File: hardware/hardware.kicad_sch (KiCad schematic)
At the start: 10 parts, among them U1 NE555P

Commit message: more research
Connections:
- net V_IN is gone; now on net KB_IN: C1.2, RV4.2, U1.5 (CV)
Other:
- note added: "555 VCO"
- note added: "Arduino Inputs"
- note added: "Keyboard simulator"
- moved on the sheet: RV4
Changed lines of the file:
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@@
     (stroke (width 0) (type default) (color 0 0 0 0))
   )
-  (wire (pts (xy 160.02 81.28) (xy 162.56 81.28))
+  (wire (pts (xy 168.275 67.945) (xy 170.815 67.945))
     (stroke (width 0) (type default) (color 0 0 0 0))
   )
@@
     (stroke (width 0) (type default) (color 0 0 0 0))
   )
+  (text "Keyboard simulator" (at 168.91 74.295 0)
+    (effects (font (size 1.27 1.27)) (justify left bottom))
+  )
+  (text "555 VCO\n" (at 74.93 86.995 0)
+    (effects (font (size 1.27 1.27)) (justify left bottom))
+  )
+  (text "Arduino Inputs" (at 85.09 26.035 0)
+    (effects (font (size 1.27 1.27)) (justify left bottom))
+  )
   (global_label "POT_REL" (shape input) (at 55.88 54.61 0) (fields_autoplaced)
     (effects (font (size 1.27 1.27)) (justify left))
@@
     )
   )
-  (global_label "V_IN" (shape input) (at 87.63 71.12 180) (fields_autoplaced)
+  (global_label "KB_IN" (shape input) (at 87.63 71.12 180) (fields_autoplaced)
     (effects (font (size 1.27 1.27)) (justify right))
-    (property "Intersheet References" "${INTERSHEET_REFS}" (id 0) (at 81.2255 71.0406 0)
+    (property "Intersheet References" "${INTERSHEET_REFS}" (id 0) (at 79.774 71.0406 0)
       (effects (font (size 1.27 1.27)) (justify right) hide)
     )
@@
     )
   )
-  (global_label "V_IN" (shape output) (at 162.56 81.28 0) (fields_autoplaced)
-    (effects (font (size 1.27 1.27)) (justify left))
-    (property "Intersheet References" "${INTERSHEET_REFS}" (id 0) (at 168.9645 81.2006 0)
+  (global_label "KB_IN" (shape output) (at 170.815 67.945 0) (fields_autoplaced)
+    (effects (font (size 1.27 1.27)) (justify left))
+    (property "Intersheet References" "${INTERSHEET_REFS}" (id 0) (at 178.671 67.8656 0)
       (effects (font (size 1.27 1.27)) (justify left) hide)
     )
@@
     )
   )
-  (symbol (lib_id "Device:R_Potentiometer") (at 156.21 81.28 0) (unit 1)
-    (in_bom yes) (on_board yes) (fields_autoplaced)
-    (property "Reference" "RV4" (id 0) (at 153.67 80.0099 0)
-      (effects (font (size 1.27 1.27)) (justify right))
-    )
-    (property "Value" ">10k" (id 1) (at 153.67 82.5499 0)
-      (effects (font (size 1.27 1.27)) (justify right))
-    )
-    (property "Footprint" "" (id 2) (at 156.21 81.28 0)
-      (effects (font (size 1.27 1.27)) hide)
-    )
-    (property "Datasheet" "~" (id 3) (at 156.21 81.28 0)
+  (symbol (lib_id "Device:R_Potentiometer") (at 164.465 67.945 0) (unit 1)
+    (in_bom yes) (on_board yes) (fields_autoplaced)
+    (property "Reference" "RV4" (id 0) (at 161.925 66.6749 0)
+      (effects (font (size 1.27 1.27)) (justify right))
+    )
+    (property "Value" ">10k" (id 1) (at 161.925 69.2149 0)
+      (effects (font (size 1.27 1.27)) (justify right))
+    )
+    (property "Footprint" "" (id 2) (at 164.465 67.945 0)
+      (effects (font (size 1.27 1.27)) hide)
+    )
+    (property "Datasheet" "~" (id 3) (at 164.465 67.945 0)
       (effects (font (size 1.27 1.27)) hide)
     )
@@
     (pin "1")
   )
-  (symbol (lib_id "power:VCC") (at 156.21 77.47 0) (unit 1)
-    (in_bom yes) (on_board yes) (fields_autoplaced)
-    (property "Reference" "#PWR?" (id 0) (at 156.21 81.28 0)
-      (effects (font (size 1.27 1.27)) hide)
-    )
-    (property "Value" "VCC" (id 1) (at 156.21 71.755 0))
-    (property "Footprint" "" (id 2) (at 156.21 77.47 0)
-      (effects (font (size 1.27 1.27)) hide)
-    )
-    (property "Datasheet" "" (id 3) (at 156.21 77.47 0)
+  (symbol (lib_id "power:VCC") (at 164.465 64.135 0) (unit 1)
+    (in_bom yes) (on_board yes) (fields_autoplaced)
+    (property "Reference" "#PWR?" (id 0) (at 164.465 67.945 0)
+      (effects (font (size 1.27 1.27)) hide)
+    )
+    (property "Value" "VCC" (id 1) (at 164.465 58.42 0))
+    (property "Footprint" "" (id 2) (at 164.465 64.135 0)
+      (effects (font (size 1.27 1.27)) hide)
+    )
+    (property "Datasheet" "" (id 3) (at 164.465 64.135 0)
       (effects (font (size 1.27 1.27)) hide)
     )
@@
     (pin "2")
   )
-  (symbol (lib_id "power:GND") (at 156.21 85.09 0) (unit 1)
-    (in_bom yes) (on_board yes) (fields_autoplaced)
-    (property "Reference" "#PWR?" (id 0) (at 156.21 91.44 0)
-      (effects (font (size 1.27 1.27)) hide)
-    )
-    (property "Value" "GND" (id 1) (at 156.21 90.17 0))
-    (property "Footprint" "" (id 2) (at 156.21 85.09 0)
-      (effects (font (size 1.27 1.27)) hide)
-    )
-    (property "Datasheet" "" (id 3) (at 156.21 85.09 0)
-      (effects (font (size 1.27 1.27)) hide)
-    )
+  (symbol (lib_id "power:GND") (at 164.465 71.755 0) (unit 1)
+    (in_bom yes) (on_board yes) (fields_autoplaced)
+    (property "Reference" "#PWR?" (id 0) (at 164.465 78.105 0)
+      (effects (font (size 1.27 1.27)) hide)
+    )
+    (property "Value" "GND" (id 1) (at 164.465 76.835 0))
+    (property "Footprint" "" (id 2) (at 164.465 71.755 0)
+      (effects (font (size 1.27 1.27)) hide)
+    )
+    (property "Datasheet" "" (id 3) (at 164.465 71.755 0)
+      (effects (font (size 1.27 1.27)) hide)
+    )

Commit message: more test schematics
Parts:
- added C4: 0.1u, symbol Device:C
- added C5: 10u, symbol Device:C
- added R9: KB_R, symbol Device:R_Variable
- added U2: NE555P, Package_DIP:DIP-8_W7.62mm, symbol Timer:NE555P
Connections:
- net GND: now also C4.1, C5.2, U2.1 (GND)
- net VCC: now also C4.2, U2.4 (R), U2.8 (VCC)
- new net: C5.1, R9.1, U2.2 (TR), U2.6 (THR)
- new net: R9.2, U2.3 (Q)
- no-connect marks 2 -> 4
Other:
- note added: "555 RCO"
- moved on the sheet: RV4

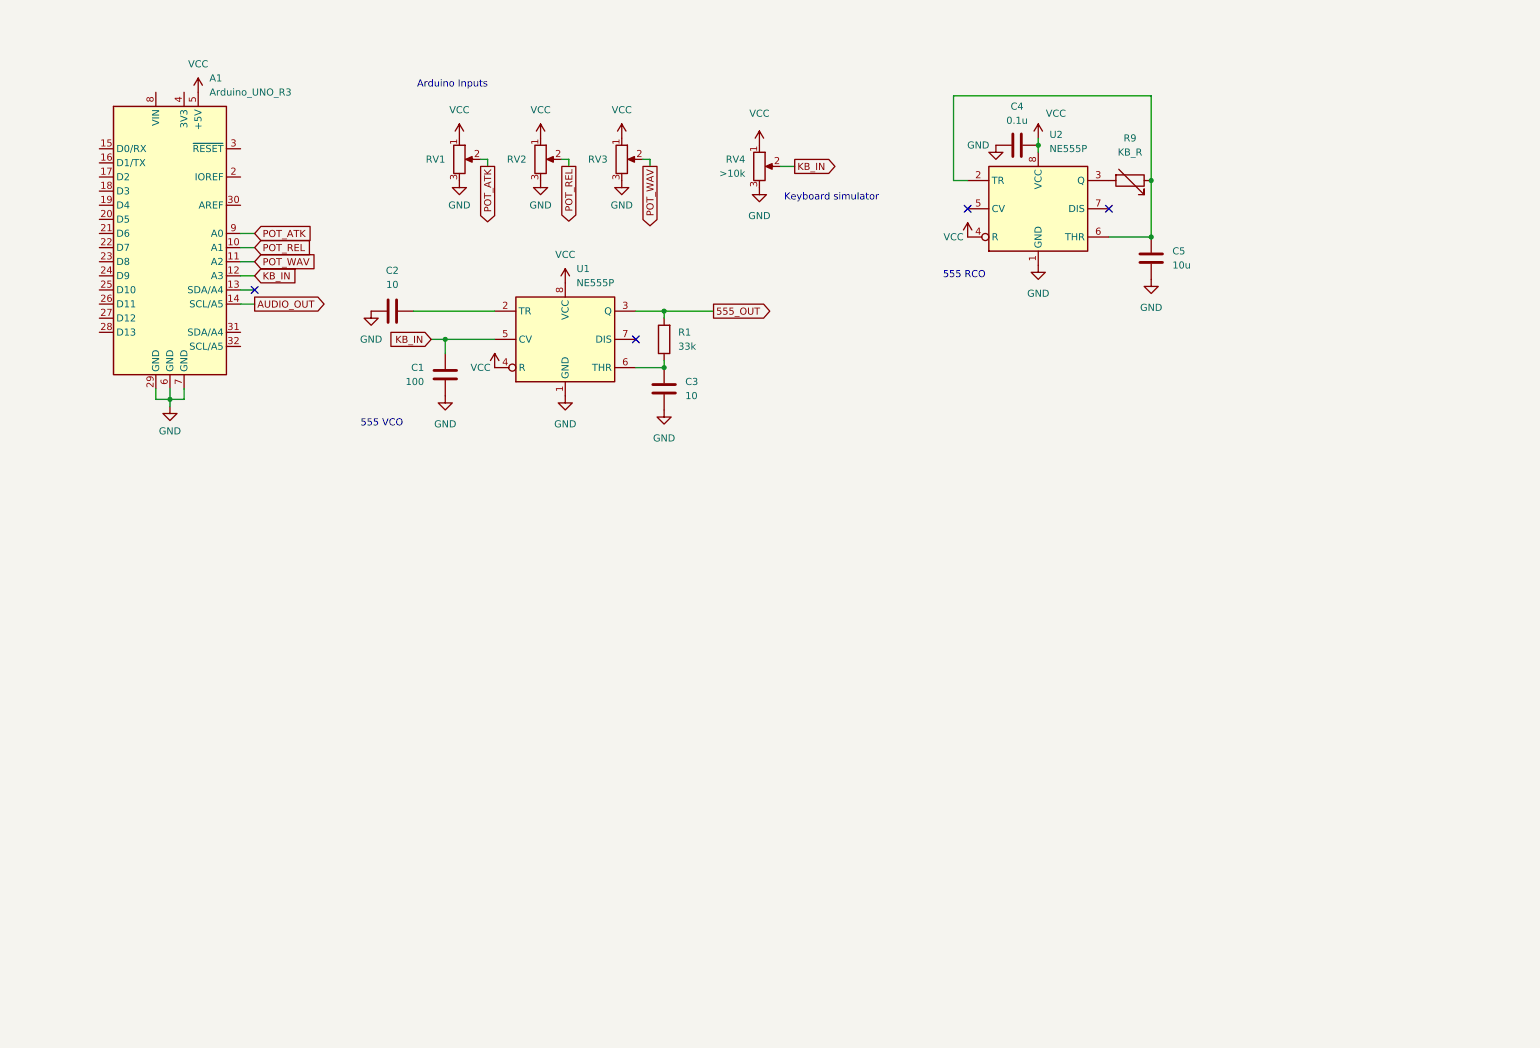
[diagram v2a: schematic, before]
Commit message: partitioning schematics
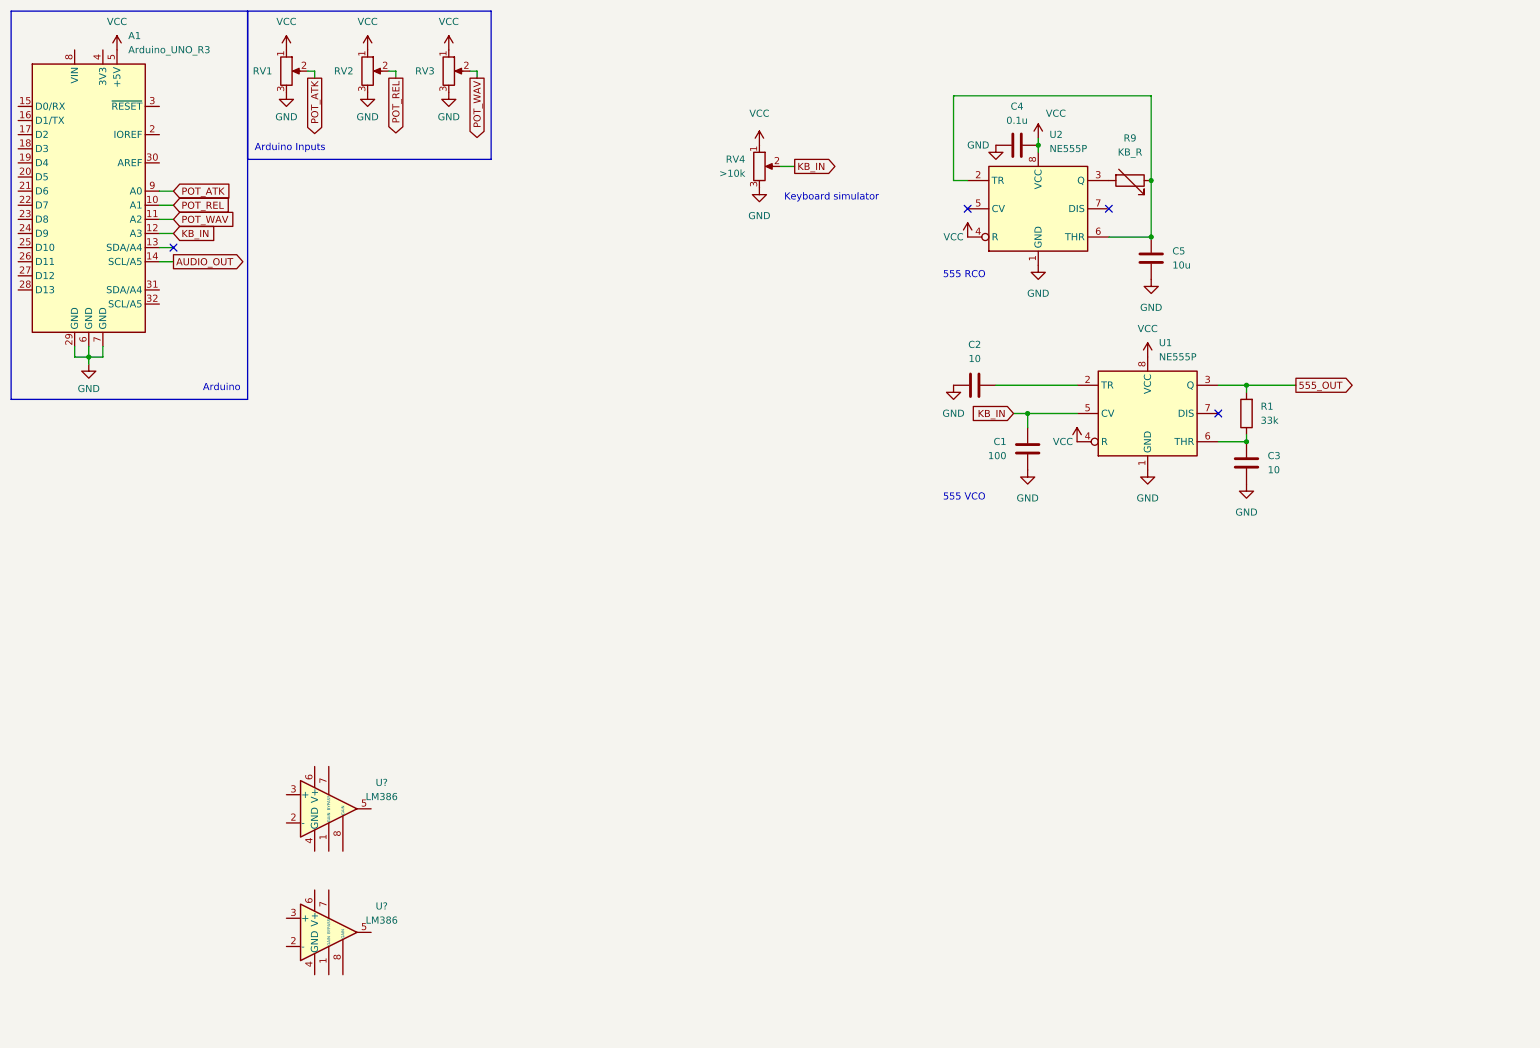
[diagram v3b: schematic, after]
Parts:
- added U? (x2): LM386, symbol Amplifier_Audio:LM386
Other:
- note added: "Arduino"
- moved on the sheet: A1, C1, C2, C3, R1, RV1, RV2, RV3, U1

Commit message: mode hardware tests
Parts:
- removed C1: 100, symbol Device:C
- removed C2: 10, symbol Device:C
- removed R1: 33k, symbol Device:R
- removed U1: NE555P, Package_DIP:DIP-8_W7.62mm, symbol Timer:NE555P
- removed U?: LM386, symbol Amplifier_Audio:LM386
- added C4: 1000u, symbol Device:C
- added C5: 100u, symbol Device:C
- added C6, C7: 100n, symbol Device:C
- added C8: 10n, symbol Device:C
- added R2: 33k, symbol Device:R
- added RV4, RV5: 10k, symbol Device:R_Potentiometer
- added RV7: CV_PITCH, symbol Device:R_Potentiometer
- added U3: NE555P, Package_DIP:DIP-8_W7.62mm, symbol Timer:NE555P
- C1: renamed from C4; value 0.1u -> 100n
- C3: value 10 -> 100n
- RV1, RV2, RV3: value R_Potentiometer -> 10k
- RV6: renamed from RV4; value >10k -> 10k
- gave numbers to parts that had none: 1
- renumbered C5 to C2, R9 to R1, U2 to U1
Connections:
- net AUDIO_OUT: now also C4.2; no longer A1.14 (SCL/A5)
- net GND: now also C3.1, U2.4 (GND), C5.2, C6.1, C7.2, C8.2, RV4.3, RV5.3, RV7.3, U3.1 (GND); no longer C3.2
- net VCC: now also C3.2, U2.6 (V+), C6.2, RV4.1, RV5.1, RV7.1, U3.4 (R), U3.8 (VCC)
- net at U2.5: now also C4.1, C5.1
- new net: C7.1, RV7.2, U3.5 (CV)
- new net: C8.1, R2.2, U3.2 (TR), U3.6 (THR)
- new net D_SYNTH: A1.14 (SCL/A5)
- new net OUT: R2.1, U3.3 (Q)
- new net POT_MIX: RV5.2
- new net POT_VOL: RV4.2
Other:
- added sheet 555 vco (555_vco.kicad_sch)
- note added: "analog arduino input knobs"
- note added: "arduino"
- note added: "keyboard simulator"
- note added: "other analog input knobs"
- note removed: "555 VCO"
- note removed: "Arduino"
- note removed: "Arduino Inputs"
- note removed: "Keyboard simulator"
- company: (none) -> Loek Le Blansch
- title: (none) -> Stylofoon
- moved on the sheet: C1, C2, R1, RV1, RV2, RV3, RV6, U1, U2

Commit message: added lab tests
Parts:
- R2: value 33k -> 220k
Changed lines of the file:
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@@
       (effects (font (size 1.27 1.27)) (justify left))
     )
-    (property "Value" "33k" (id 1) (at 161.29 137.7949 0)
+    (property "Value" "220k" (id 1) (at 161.29 137.7949 0)
       (effects (font (size 1.27 1.27)) (justify left))
     )
@@
     )
     (path "/d80d6069-5c80-40cf-ace0-ff64c4c14177"
-      (reference "R2") (unit 1) (value "33k") (footprint "")
+      (reference "R2") (unit 1) (value "220k") (footprint "")
     )
     (path "/5b9b5460-2c14-4b59-b061-00384d4e6422/353d10af-18da-4a76-9647-8341271e9bc7"

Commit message: electric schematics and typo fix
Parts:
- removed C1: 100n, symbol Device:C
- removed C2: 10u, symbol Device:C
- removed R1: KB_R, symbol Device:R_Variable
- removed U1: NE555P, Package_DIP:DIP-8_W7.62mm, symbol Timer:NE555P
- added BAR1: HDSP-4832_2, Display:HDSP-4832, symbol LED:HDSP-4832_2
- added C7: 100n, symbol Device:C
- added C8: 2.2u, symbol Device:C
- added R1: 10k, symbol Device:R
- added R10: 1.3k, symbol Device:R
- added R11: 1.41k, symbol Device:R
- added R12: 1.37k, symbol Device:R
- added R13: 1.58k, symbol Device:R
- added R14: 1.79k, symbol Device:R
- added R15: 1.8k, symbol Device:R
- added R16: 1.92k, symbol Device:R
- added R17: 2.16k, symbol Device:R
- added R18: 2.24k, symbol Device:R
- added R19: 2.23k, symbol Device:R
- added R2: 570, symbol Device:R
- added R20: 2.86k, symbol Device:R
- added R21: 12.25k, symbol Device:R
- added R22: 100k, symbol Device:R
- added R3: 1.12k, symbol Device:R
- added R4: 600, symbol Device:R
- added R5: 790, symbol Device:R
- added R6: 1k, symbol Device:R
- added R7: 730, symbol Device:R
- added R8: 1.03k, symbol Device:R
- added R9: 1.11k, symbol Device:R
- added RV10, RV11, RV12, RV13, RV14, RV15, RV16, RV17, RV18, RV19, RV20, RV21, RV22, RV23, RV24, RV25, RV26, RV8, RV9: 50, symbol Device:R_Potentiometer
- added TP1: TUNE, symbol Connector:TestPoint
- added TP10: C#4, symbol Connector:TestPoint
- added TP11: D4, symbol Connector:TestPoint
- added TP12: D#4, symbol Connector:TestPoint
- added TP13: E4, symbol Connector:TestPoint
- added TP14: F4, symbol Connector:TestPoint
- added TP15: F#4, symbol Connector:TestPoint
- added TP16: G4, symbol Connector:TestPoint
- added TP17: G#4, symbol Connector:TestPoint
- added TP18: A4, symbol Connector:TestPoint
- added TP19: A#4, symbol Connector:TestPoint
- added TP2: F3, symbol Connector:TestPoint
- added TP20: B4, symbol Connector:TestPoint
- added TP21: C5, symbol Connector:TestPoint
- added TP22: STYLUS, symbol Connector:TestPoint_Probe
- added TP23: REF_GND, symbol Connector:TestPoint
- added TP3: F#3, symbol Connector:TestPoint
- added TP4: G3, symbol Connector:TestPoint
- added TP5: G#3, symbol Connector:TestPoint
- added TP6: A3, symbol Connector:TestPoint
- added TP7: A#3, symbol Connector:TestPoint
- added TP8: B3, symbol Connector:TestPoint
- added TP9: C4, symbol Connector:TestPoint
- added U3: LM3914V, Package_LCC:PLCC-20, symbol Driver_LED:LM3914V
- RV6: value 10k -> 200
- RV7: value CV_PITCH -> 50
- renumbered C6 to C1, C7 to C2, C8 to C5, C5 to C6, R2 to R23, U3 to U1
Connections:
- net AUDIO_OUT: now also U3.5 (SIG)
- net GND: now also C7.1, C8.2, R21.1, TP23.1, U3.2 (V-), U3.4 (RLO); no longer RV6.3, RV7.3
- net KB_IN: now also C2.1, U1.5 (CV), R22.2, TP22.1; no longer A1.12 (A3), RV6.2
- net VCC: now also C7.2, TP1.1, U3.11 (MODE), U3.3 (V+); no longer RV7.1
- net OUT renamed A_SYNTH
- new net: R17.1, RV23.1, TP18.1
- new net: R18.2, RV23.2
- new net: R18.1, RV24.1, TP19.1
- new net: R11.1, RV17.1, TP12.1
- new net: R11.2, RV16.2
- new net: R13.1, RV19.1, TP14.1
- new net: R14.2, RV19.2
- new net: R6.1, RV12.1, TP7.1
- new net: R14.1, RV20.1, TP15.1
- new net: R16.1, RV22.1, TP17.1
- new net: A1.12 (A3), R22.1
- new net: R7.1, RV13.1, TP8.1
- new net: R12.1, RV18.1, TP13.1
- new net: R12.2, RV17.2
- new net: R5.1, RV11.1, TP6.1
- new net: R5.2, RV10.2
- new net: R6.2, RV11.2
- new net: R19.1, RV25.1, TP20.1
- new net: R20.2, RV25.2
- new net: R15.1, RV21.1, TP16.1
- new net: R16.2, RV21.2
- new net: R19.2, RV24.2
- new net: R17.2, RV22.2
- new net: R4.1, RV10.1, TP5.1
- new net: R8.1, RV14.1, TP9.1
- new net: R8.2, RV13.2
- new net: R10.1, RV16.1, TP11.1
- new net: R10.2, RV15.2
- new net: BAR1.20 (K), U3.1 (LED1)
- new net: BAR1.11 (K), U3.12 (LED10)
- new net: BAR1.12 (K), U3.13 (LED9)
- new net: BAR1.13 (K), U3.14 (LED8)
- new net: BAR1.14 (K), U3.15 (LED7)
- new net: BAR1.15 (K), U3.16 (LED6)
- new net: BAR1.16 (K), U3.17 (LED5)
- new net: BAR1.17 (K), U3.18 (LED4)
- new net: BAR1.18 (K), U3.19 (LED3)
- new net: BAR1.19 (K), U3.20 (LED2)
- new net: R15.2, RV20.2
- new net: R3.1, RV9.1, TP4.1
- new net: R3.2, RV8.2
- new net: R20.1, RV26.1, TP21.1
- new net: R9.2, RV14.2
- new net: R1.1, RV7.1, TP2.1
- new net: R2.2, RV7.2
- new net: R13.2, RV18.2
- new net: R1.2, RV6.2
- new net: R7.2, RV12.2
- new net: R4.2, RV9.2
- new net: R21.2, RV26.2
- new net: R9.1, RV15.1, TP10.1
- new net: R2.1, RV8.1, TP3.1
- new net: BAR1.1 (A), BAR1.10 (A), BAR1.2 (A), BAR1.3 (A), BAR1.4 (A), BAR1.5 (A), BAR1.6 (A), BAR1.7 (A), BAR1.8 (A), BAR1.9 (A), C8.1
- no-connect marks 4 -> 22
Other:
- removed sheet 555 vco
- note added: "555 vco"
- note added: "TODO: - audio versterker afmaken - mixer - vu meter - aan/uit knop - stroom voorzieningen - stylus verbindingen"
- note added: "WIP"
- note added: "audio versterker"
- note added: "vu meter"
- note added: "weerstandsladder (keyboard)"
- note removed: "555 RCO"
- note removed: "keyboard simulator"
- moved on the sheet: C1, C2, C3, C4, C5, C6, R23, RV1, RV2, RV3, RV4, RV5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
